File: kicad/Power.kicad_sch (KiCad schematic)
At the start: 10 parts

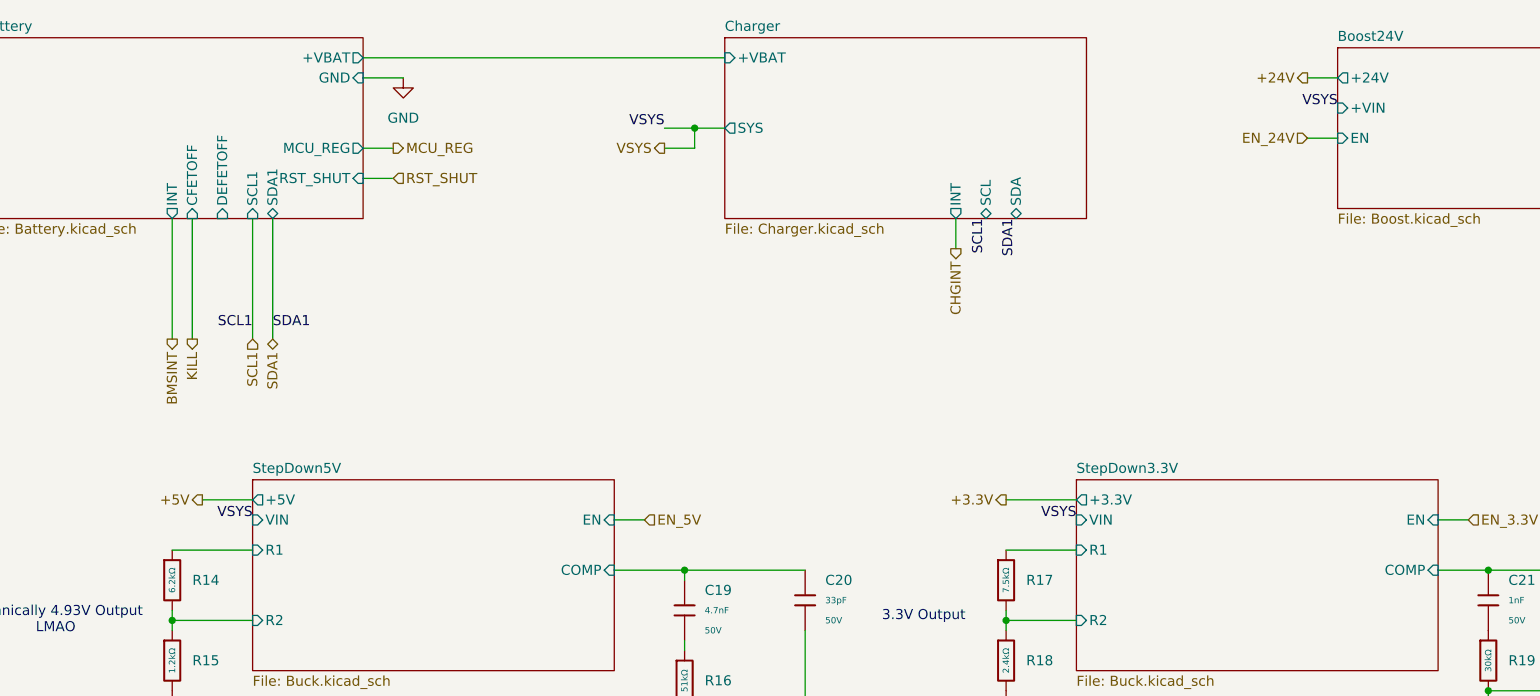
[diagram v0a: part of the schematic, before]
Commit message: Footprint routing completed
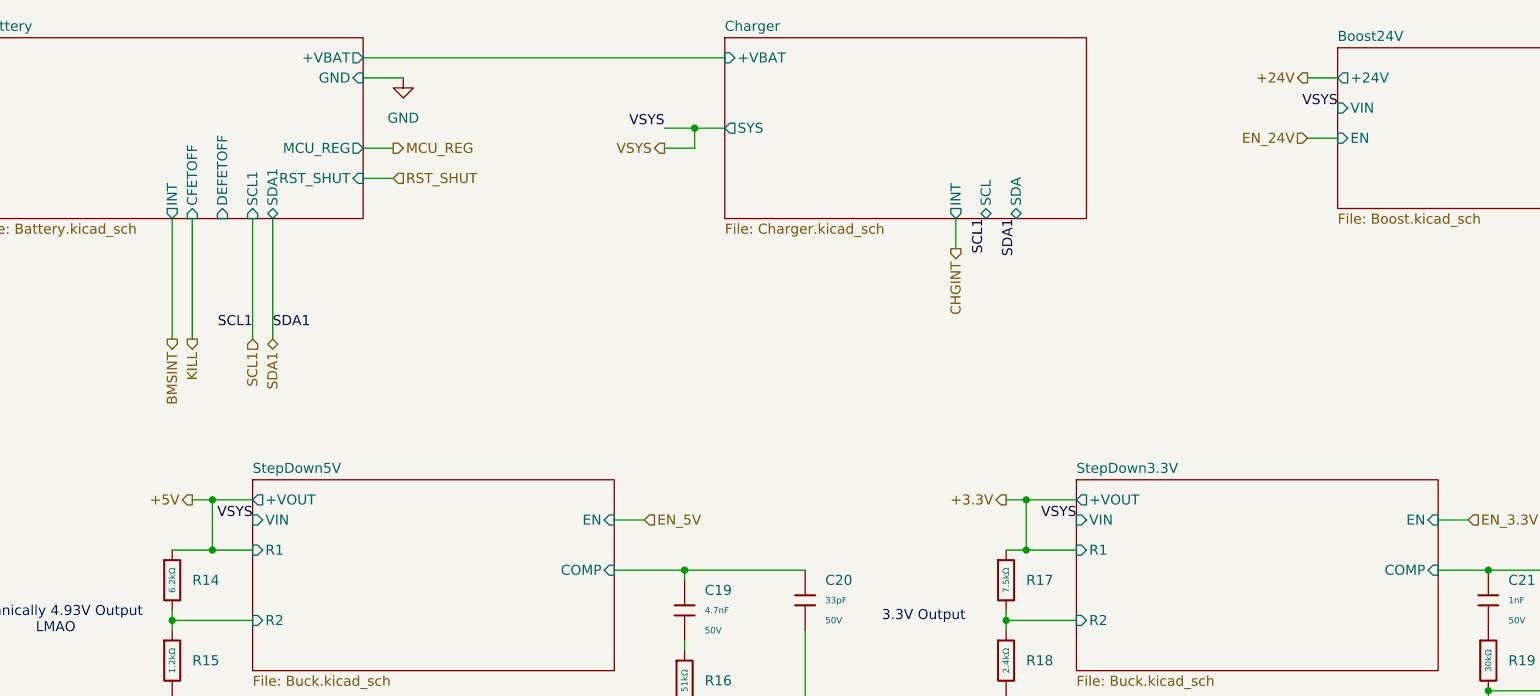
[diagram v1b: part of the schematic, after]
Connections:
- net StepDown3.3V/R1 is gone; now on net +3.3V: R17.1
- net StepDown5V/R1 is gone; now on net +5V: R14.1
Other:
- sheet Boost24V ports: added VIN; removed +VIN
- sheet StepDown3.3V ports: added +VOUT; removed +3.3V
- sheet StepDown5V ports: added +VOUT; removed +5V
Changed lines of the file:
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@@
 	)
 	(junction
+		(at 46.99 80.01)
+		(diameter 0)
+		(color 0 0 0 0)
+	)
+	(junction
+		(at 46.99 86.36)
+		(diameter 0)
+		(color 0 0 0 0)
+	)
+	(junction
+		(at 149.86 80.01)
+		(diameter 0)
+		(color 0 0 0 0)
+	)
+	(junction
 		(at 121.92 109.22)
 		(diameter 0)
@@
 	)
 	(junction
+		(at 149.86 86.36)
+		(diameter 0)
+		(color 0 0 0 0)
+	)
+	(junction
 		(at 107.95 33.02)
 		(diameter 0)
@@
 	(wire
 		(pts
-			(xy 45.72 80.01) (xy 52.07 80.01)
+			(xy 44.45 80.01) (xy 46.99 80.01)
 		)
 		(stroke
@@
 	(wire
 		(pts
+			(xy 149.86 80.01) (xy 149.86 86.36)
+		)
+		(stroke
+			(width 0)
+			(type default)
+		)
+	)
+	(wire
+		(pts
 			(xy 107.95 35.56) (xy 107.95 33.02)
 		)
@@
 	(wire
 		(pts
-			(xy 41.91 86.36) (xy 52.07 86.36)
+			(xy 46.99 80.01) (xy 46.99 86.36)
+		)
+		(stroke
+			(width 0)
+			(type default)
+		)
+	)
+	(wire
+		(pts
+			(xy 149.86 80.01) (xy 156.21 80.01)
+		)
+		(stroke
+			(width 0)
+			(type default)
+		)
+	)
+	(wire
+		(pts
+			(xy 41.91 86.36) (xy 46.99 86.36)
 		)
 		(stroke
@@
 	(wire
 		(pts
-			(xy 147.32 86.36) (xy 156.21 86.36)
+			(xy 147.32 86.36) (xy 149.86 86.36)
 		)
 		(stroke
@@
 	(wire
 		(pts
-			(xy 147.32 80.01) (xy 156.21 80.01)
+			(xy 147.32 80.01) (xy 149.86 80.01)
 		)
 		(stroke
@@
 	(wire
 		(pts
+			(xy 46.99 80.01) (xy 52.07 80.01)
+		)
+		(stroke
+			(width 0)
+			(type default)
+		)
+	)
+	(wire
+		(pts
 			(xy 52.07 44.45) (xy 52.07 59.69)
 		)
@@
 	(wire
 		(pts
+			(xy 149.86 86.36) (xy 156.21 86.36)
+		)
+		(stroke
+			(width 0)
+			(type default)
+		)
+	)
+	(wire
+		(pts
 			(xy 205.74 82.55) (xy 201.93 82.55)
 		)
@@
 	(wire
 		(pts
+			(xy 46.99 86.36) (xy 52.07 86.36)
+		)
+		(stroke
+			(width 0)
+			(type default)
+		)
+	)
+	(wire
+		(pts
 			(xy 69.85 35.56) (xy 66.04 35.56)
 		)
@@
 	(hierarchical_label "+5V"
 		(shape output)
-		(at 45.72 80.01 180)
+		(at 44.45 80.01 180)
 		(effects
 			(font
@@
 			)
 		)
-		(pin "+3.3V" output
-			(at 156.21 80.01 180)
-			(effects
-				(font
-					(size 1.27 1.27)
-				)
-				(justify left)
-			)
-		)
 		(pin "R1" input
 			(at 156.21 86.36 180)
@@
 			)
 		)
+		(pin "+VOUT" output
+			(at 156.21 80.01 180)
+			(effects
+				(font
+					(size 1.27 1.27)
+				)
+				(justify left)
+			)
+		)
 		(instances
 			(project "4-in-power-improved"
@@
 			)
 		)
-		(pin "+VIN" input
-			(at 189.23 30.48 180)
+		(pin "EN" input
+			(at 189.23 34.29 180)
 			(effects
 				(font
@@
 			)
 		)
-		(pin "EN" input
-			(at 189.23 34.29 180)
+		(pin "VIN" input
+			(at 189.23 30.48 180)
 			(effects
 				(font
@@
 			)
 		)
-		(pin "+5V" output
-			(at 52.07 80.01 180)
-			(effects
-				(font
-					(size 1.27 1.27)
-				)
-				(justify left)
-			)
-		)
 		(pin "R1" input
 			(at 52.07 86.36 180)
@@
 			(effects
 				(font
+					(size 1.27 1.27)
+				)
+				(justify left)
+			)
+		)
+		(pin "+VOUT" output
+			(at 52.07 80.01 180)
+			(effects
+				(font
